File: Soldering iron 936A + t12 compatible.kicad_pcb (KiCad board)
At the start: 2 copper layers, 97 x 67 mm, 69 parts, among them J1 DC INPUT, J2 OLED, J3 AC input, J4 output_connector, J5 mosfet_driver_future_backup, J6 OLED, Q1 IRF9540N, Q2 BC547, SW1 RotaryEncoder_Switch, U1 LM2596S-ADJ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

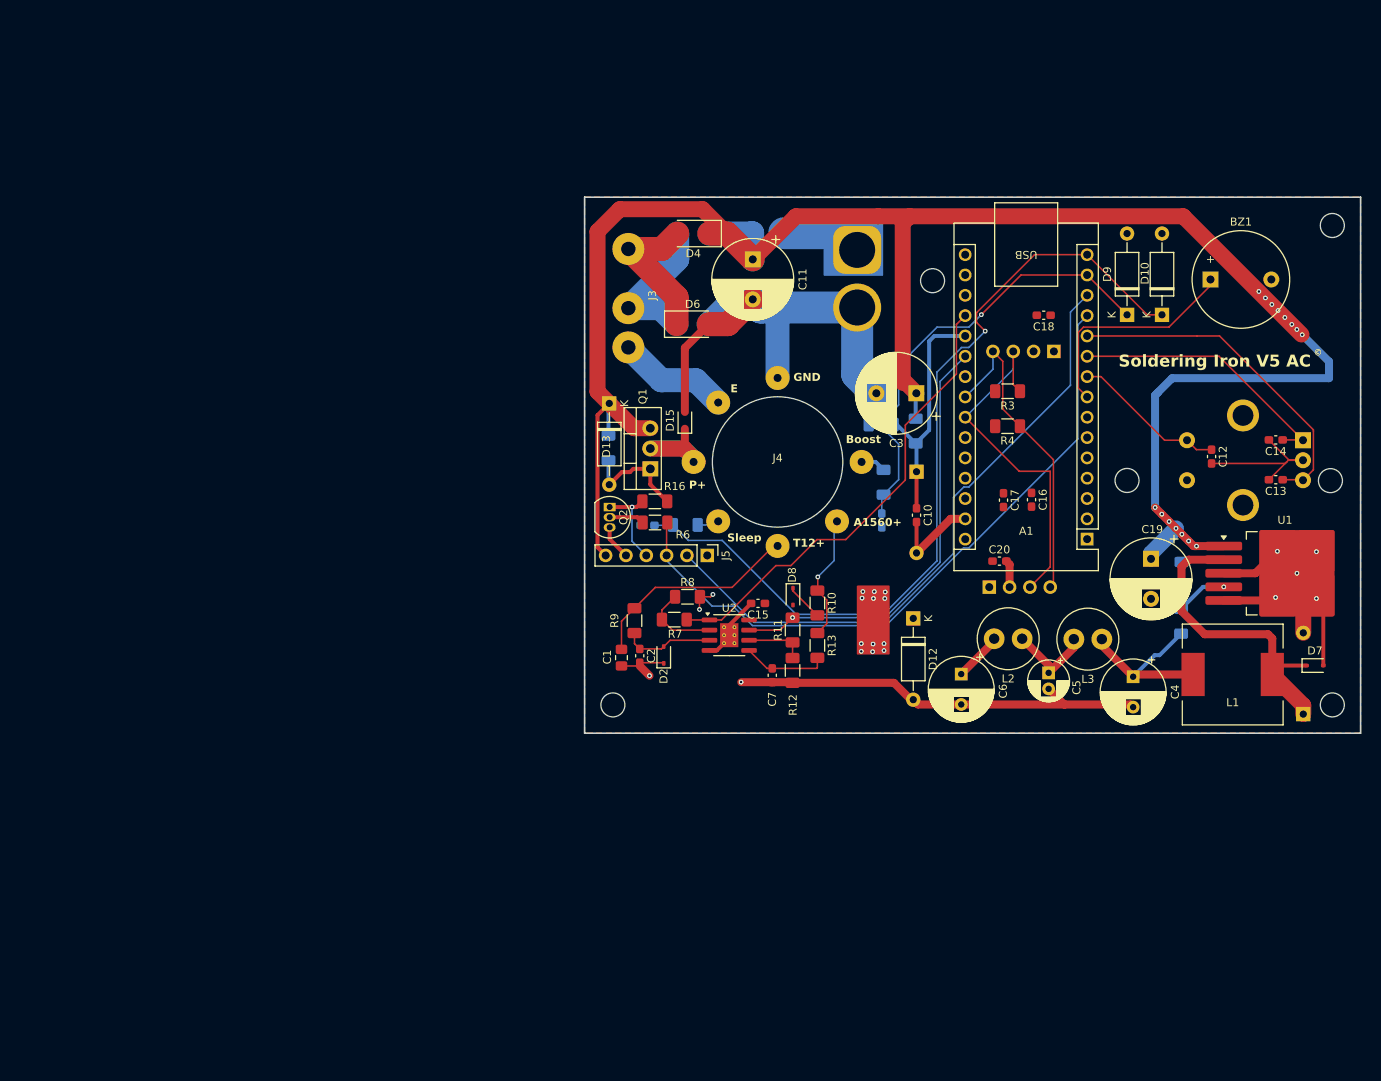
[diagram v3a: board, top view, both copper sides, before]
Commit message: added all 3d model files , almost finalised schematic , rough placment of big components
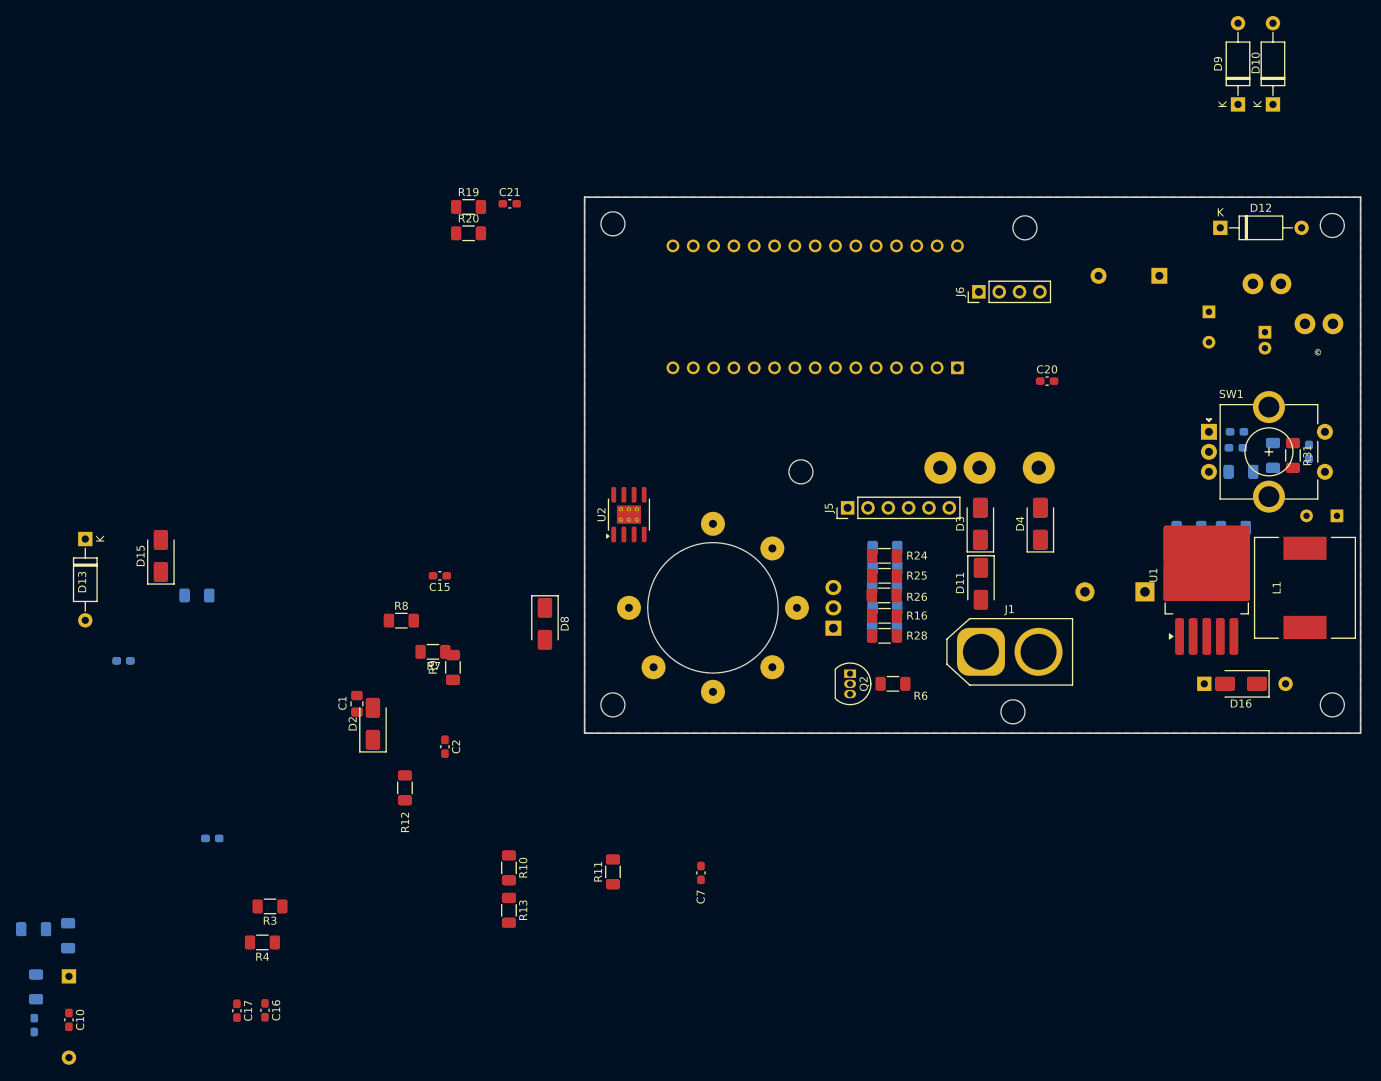
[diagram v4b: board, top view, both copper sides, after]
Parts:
- removed C11, C3: 1000uF, Capacitor_THT:CP_Radial_D10.0mm_P5.00mm
- removed D7: 1N5817WS, Diode_SMD:D_SOD-323
- removed J2: OLED, Connector_PinHeader_2.54mm:PinHeader_1x04_P2.54mm_Vertical
- added C21: 100nf, Capacitor_SMD:C_0603_1608Metric_Pad1.08x0.95mm_HandSolder, F.Cu at (161.6, 67.0)
- added D16: SS310, Diode_SMD:D_SMA, F.Cu at (253.0, 127.0)
- added R19: 5M, Resistor_SMD:R_1206_3216Metric_Pad1.30x1.75mm_HandSolder, F.Cu at (156.4, 67.4)
- added R20: 100, Resistor_SMD:R_1206_3216Metric_Pad1.30x1.75mm_HandSolder, F.Cu at (156.4, 70.7)
- added R21: 1.5k, Resistor_SMD:R_1206_3216Metric_Pad1.30x1.75mm_HandSolder, B.Cu at (208.5, 110.0)
- added R22: 1.5k, Resistor_SMD:R_1206_3216Metric_Pad1.30x1.75mm_HandSolder, B.Cu at (208.5, 112.5)
- added R23: 1.5k, Resistor_SMD:R_1206_3216Metric_Pad1.30x1.75mm_HandSolder, B.Cu at (208.4, 115.0)
- added R24: 3.3k, Resistor_SMD:R_1206_3216Metric_Pad1.30x1.75mm_HandSolder, F.Cu at (208.4, 111.0)
- added R25: 3.3k, Resistor_SMD:R_1206_3216Metric_Pad1.30x1.75mm_HandSolder, F.Cu at (208.4, 113.5)
- added R26: 3.3k, Resistor_SMD:R_1206_3216Metric_Pad1.30x1.75mm_HandSolder, F.Cu at (208.4, 116.0)
- added R27: 1.5k, Resistor_SMD:R_1206_3216Metric_Pad1.30x1.75mm_HandSolder, B.Cu at (208.5, 117.5)
- added R28: 3.3k, Resistor_SMD:R_1206_3216Metric_Pad1.30x1.75mm_HandSolder, F.Cu at (208.4, 121.0)
- added R29: 5k, Resistor_SMD:R_1206_3216Metric_Pad1.30x1.75mm_HandSolder, B.Cu at (257.0, 98.5)
- added R30: 5k, Resistor_SMD:R_1206_3216Metric_Pad1.30x1.75mm_HandSolder, B.Cu at (253.0, 100.5)
- added R31: 5k, Resistor_SMD:R_1206_3216Metric_Pad1.30x1.75mm_HandSolder, F.Cu at (259.5, 98.5)
- A1, BZ1, C12, C13, C14, C18, C4, C5, C6, D6, J3, J4, L2, L3, Q1: moved to B.Cu
- C19: footprint Capacitor_THT:CP_Radial_D10.0mm_P5.00mm -> Capacitor_THT:CP_Radial_D16.0mm_P7.50mm; moved to B.Cu
- D11, D3, J1, J6, SW1: moved to F.Cu
- D15, D2, D8: value 1N5817WS -> SS310; footprint Diode_SMD:D_SOD-323 -> Diode_SMD:D_SMA
- R16: value 10k -> 3.3k
- R5: value 10k -> 1.5k
- moved C8 123.3 mm to (102.2, 169.7)
- moved R2 123.3 mm to (106.4, 158.5)
- moved C10 123.3 mm to (106.5, 169.0)
- moved D1 123.3 mm to (106.5, 163.6)
- moved R1 123.3 mm to (102.1, 157.7)
- moved R14 123.3 mm to (102.4, 164.9)
- moved C18 122.8 mm to (124.4, 146.3), turned to 0 degrees
- moved C17 115.1 mm to (127.5, 167.9)
- moved C16 115.1 mm to (131.0, 167.8)
- moved R4 113.3 mm to (130.7, 159.3)
- moved R3 112.5 mm to (131.6, 154.8)
- moved C9 67.7 mm to (113.3, 124.1)
- moved D15 67.7 mm to (118.0, 111.0)
- moved D13 67.7 mm to (108.5, 108.9)
- moved D12 62.1 mm to (250.4, 70.0), turned to 0 degrees
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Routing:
- net /VIN: track 268.5 -> 0.00 mm, vias 15 -> 0
- net GND: track 200.1 -> 0.00 mm, vias 21 -> 0
- net Net-(A1-D12): track 106.5 -> 0.00 mm, vias 1 -> 0
- net /PWM: track 85.1 -> 0.00 mm
- net /PWM1: track 79.9 -> 0.00 mm
- net /temp_readback: track 58.2 -> 0.00 mm
- net Net-(A1-D11): track 56.0 -> 0.00 mm, vias 1 -> 0
- net /temp_readback_2: track 54.4 -> 0.00 mm, vias 1 -> 0
- net /SCL: track 45.0 -> 0.00 mm
- net /ENCODER B: track 42.6 -> 0.00 mm
- net /SDA: track 39.9 -> 0.00 mm
- net Net-(D14-K): track 39.8 -> 0.00 mm
- net /ENCODER A: track 33.9 -> 0.00 mm
- net /VIN_ADC: track 30.1 -> 0.00 mm
- net /BUZZER: track 28.2 -> 0.00 mm
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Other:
- outline, holes or cut-outs redrawn
- board text removed: "A1560+"
- board text removed: "Boost"
- board text removed: "E"
- board text removed: "GND"
- board text removed: "P+"
- board text removed: "Sleep"
- board text removed: "T12+"

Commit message: Finalised schematic , placement
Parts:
- added 5V1: TestPoint, TestPoint:TestPoint_Pad_D1.0mm, B.Cu at (229.5, 69.0)
- added C11: 100nf, Capacitor_SMD:C_0603_1608Metric_Pad1.08x0.95mm_HandSolder, F.Cu at (202.4, 128.5)
- added C22: 1nf, Capacitor_SMD:C_0603_1608Metric_Pad1.08x0.95mm_HandSolder, F.Cu at (204.1, 131.0)
- added C23: 100nf, Capacitor_SMD:C_0603_1608Metric_Pad1.08x0.95mm_HandSolder, B.Cu at (197.6, 132.0)
- added C24: 1000uF, Capacitor_THT:CP_Radial_D16.0mm_P7.50mm, B.Cu at (243.0, 97.5)
- added C25: 100nf, Capacitor_SMD:C_0603_1608Metric_Pad1.08x0.95mm_HandSolder, F.Cu at (174.0, 96.5)
- added C26: 1uF, Capacitor_SMD:C_0603_1608Metric_Pad1.08x0.95mm_HandSolder, F.Cu at (191.4, 100.0)
- added D17: SS310, Diode_SMD:D_SMA, B.Cu at (192.5, 100.0)
- added D18: SS310, Diode_SMD:D_SMA, B.Cu at (203.5, 98.0)
- added D19: SS310, Diode_SMD:D_SMA, F.Cu at (196.0, 105.0)
- added D7: SS310, Diode_SMD:D_SMA, B.Cu at (177.0, 100.0)
- added F1: Fuse, Fuse:Fuse_1206_3216Metric_Pad1.42x1.75mm_HandSolder, F.Cu at (209.6, 101.5)
- added GND1: TestPoint, TestPoint:TestPoint_Pad_D1.0mm, B.Cu at (233.5, 69.0)
- added J2: USB TO SERIAL, Connector_PinHeader_2.54mm:PinHeader_1x04_P2.54mm_Vertical, B.Cu at (173.5, 76.0)
- added J7: USB C BREAKOUT BOARD, Connector_PinHeader_2.54mm:PinHeader_1x08_P2.54mm_Vertical, F.Cu at (194.6, 96.0)
- added PWM1: TestPoint, TestPoint:TestPoint_Pad_D1.0mm, B.Cu at (190.5, 92.0)
- added R32: 22.6K, Resistor_SMD:R_1206_3216Metric_Pad1.30x1.75mm_HandSolder, F.Cu at (183.0, 100.5)
- added R33: 10k, Resistor_SMD:R_1206_3216Metric_Pad1.30x1.75mm_HandSolder, F.Cu at (186.3, 100.5)
- added R34: 5.1K, Resistor_SMD:R_1206_3216Metric_Pad1.30x1.75mm_HandSolder, B.Cu at (175.4, 92.5)
- added R35: 1M, Resistor_SMD:R_1206_3216Metric_Pad1.30x1.75mm_HandSolder, F.Cu at (209.6, 98.5)
- added R36: 220k, Resistor_SMD:R_1206_3216Metric_Pad1.30x1.75mm_HandSolder, B.Cu at (209.4, 101.5)
- added R37: 10K, Resistor_SMD:R_1206_3216Metric_Pad1.30x1.75mm_HandSolder, F.Cu at (200.5, 91.5)
- added R38: 5.1K, Resistor_SMD:R_1206_3216Metric_Pad1.30x1.75mm_HandSolder, B.Cu at (185.4, 92.5)
- added SCL1: TestPoint, TestPoint:TestPoint_Pad_D1.0mm, B.Cu at (224.5, 74.5)
- added SDA1: TestPoint, TestPoint:TestPoint_Pad_D1.0mm, B.Cu at (228.0, 74.5)
- added U3: ACS712xLCTR-05B, Package_SO:SOIC-8_3.9x4.9mm_P1.27mm, B.Cu at (202.4, 128.0)
- added U4: HUSB238, Package_DFN_QFN:DFN-10-1EP_3x3mm_P0.5mm_EP1.58x2.35mm, B.Cu at (184.9, 101.1)
- added U5: PC817, Package_DIP:DIP-4_W7.62mm, F.Cu at (202.0, 101.5)
- added VBUS1: TestPoint, TestPoint:TestPoint_Pad_D1.0mm, B.Cu at (189.5, 105.5)
- C1, C15, C2, C21, D15, D2, J5, Q2, R20, R6: moved to B.Cu
- D1, R1, R14, R15, R2: moved to F.Cu
- D13: footprint Diode_THT:D_A-405_P10.16mm_Horizontal -> Diode_THT:D_A-405_P2.54mm_Vertical_KathodeUp; moved to B.Cu
- moved C10 143.2 mm to (235.6, 107.0), turned to 180 degrees
- moved R1 141.8 mm to (235.4, 109.5)
- moved R2 141.3 mm to (239.5, 111.1), turned to 90 degrees
- moved R4 123.6 mm to (228.0, 83.0), turned to -90 degrees
- moved C17 123.0 mm to (208.5, 75.4)
- moved D1 122.0 mm to (192.4, 77.0), turned to 0 degrees
- moved C16 121.9 mm to (210.5, 75.4)
- moved R3 118.2 mm to (225.5, 83.0), turned to -90 degrees
- moved C18 117.1 mm to (221.6, 81.0)
- moved D13 91.0 mm to (199.5, 110.5)
- moved D15 90.6 mm to (207.0, 128.0), turned to -90 degrees
- moved C8 87.9 mm to (176.0, 122.0), turned to 90 degrees
- moved R14 85.2 mm to (176.0, 122.1)
- moved C9 82.6 mm to (195.9, 128.0)
- moved D10 81.9 mm to (181.0, 85.1)
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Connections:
- A1 pad 22: unconnected-(A1-A3-Pad22) -> /current_sense
- A1 pad 7: unconnected-(A1-D4-Pad7) -> /LEAK_ERR
- D15 pad 1: /P+ -> /MOS_OUT
- J4 pad 6: Earth -> Net-(D18-A)
- Q1 pad 2: /P+ -> /MOS_OUT
- R20 pad 1: /P+ -> /MOS_OUT
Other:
- outline, holes or cut-outs redrawn

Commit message: Almost completed layout , checks pending
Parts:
- C10, F1, R1, R2, R37: moved to B.Cu
- R36: value 220k -> 50K; moved to F.Cu
- moved R2 25.2 mm to (242.2, 86.0)
- moved R1 23.8 mm to (239.5, 86.0), turned to -90 degrees
- moved C10 20.4 mm to (237.0, 86.7), turned to 90 degrees
- moved D2 13.1 mm to (181.5, 131.0), turned to 180 degrees
- moved D14 9.83 mm to (258.2, 127.0), turned to 180 degrees
- moved C19 5.67 mm to (237.0, 111.5), turned to -90 degrees
- moved C1 5.00 mm to (188.0, 131.0), turned to 0 degrees
- moved C26 2.41 mm to (189.0, 99.5), turned to 90 degrees
- moved VBUS1 1.58 mm to (191.0, 105.0)
- moved R37 0.75 mm to (200.5, 90.8)
- moved R36 0.05 mm to (209.5, 101.5)
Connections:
- U4 pad 2: Net-(D17-K) -> unconnected-(U4-D+-Pad2)
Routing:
- net /current_sense: track 0.00 -> 116.4 mm
- net /VIN: track 0.00 -> 115.7 mm, vias 0 -> 3
- net /SDA: track 0.00 -> 107.8 mm, vias 0 -> 2
- net /SCL: track 0.00 -> 101.4 mm, vias 0 -> 2
- net /PWM: track 0.00 -> 85.9 mm
- net Net-(A1-D12): track 0.00 -> 83.6 mm, vias 0 -> 3
- net /ENCODER S: track 0.00 -> 76.8 mm
- net /ENCODER B: track 0.00 -> 68.2 mm
- net /ENCODER A: track 0.00 -> 66.8 mm
- net GND: track 0.00 -> 62.0 mm, vias 0 -> 64
- net /VIN_ADC: track 0.00 -> 60.4 mm
- net Net-(A1-D11): track 0.00 -> 56.3 mm
- net /BUZZER: track 0.00 -> 51.3 mm
- net /temp_readback: track 0.00 -> 47.7 mm
- net /temp_readback_2: track 0.00 -> 44.3 mm
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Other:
- outline, holes or cut-outs redrawn

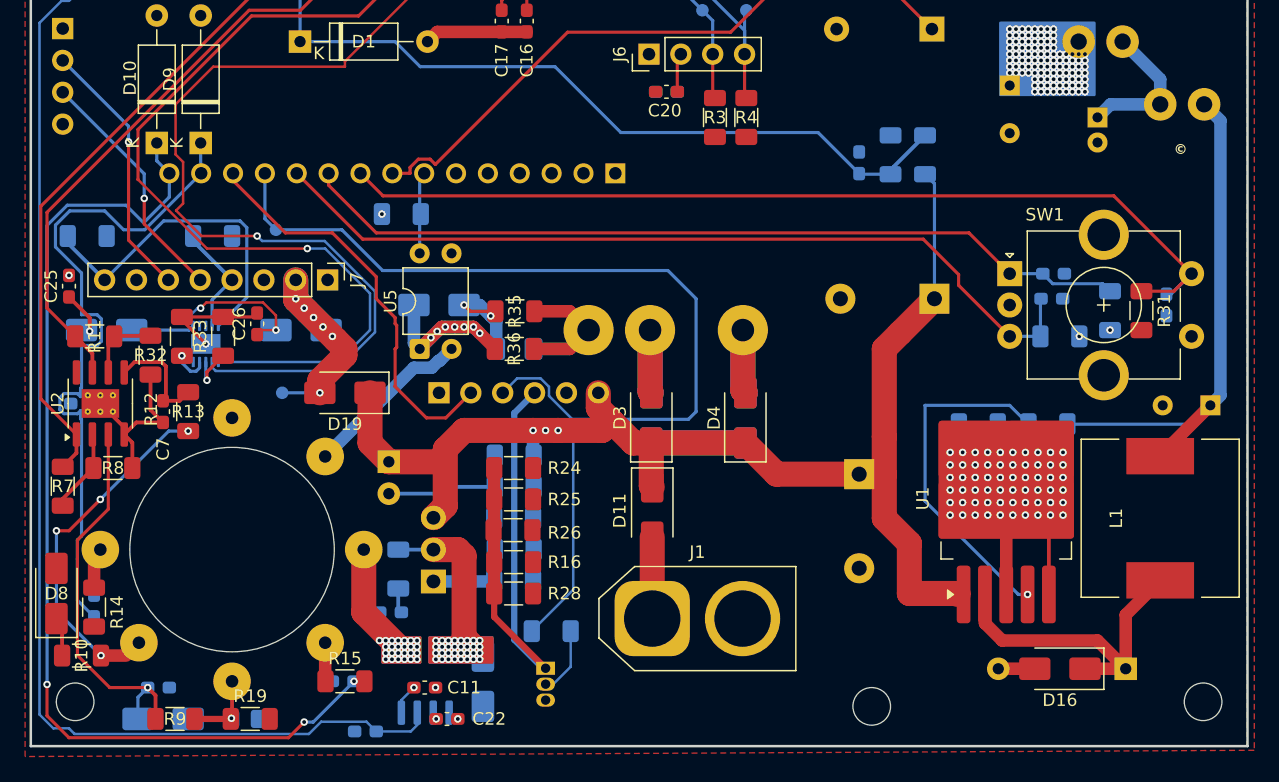
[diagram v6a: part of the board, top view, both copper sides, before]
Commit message: Layout fully complete yet to be reviewed
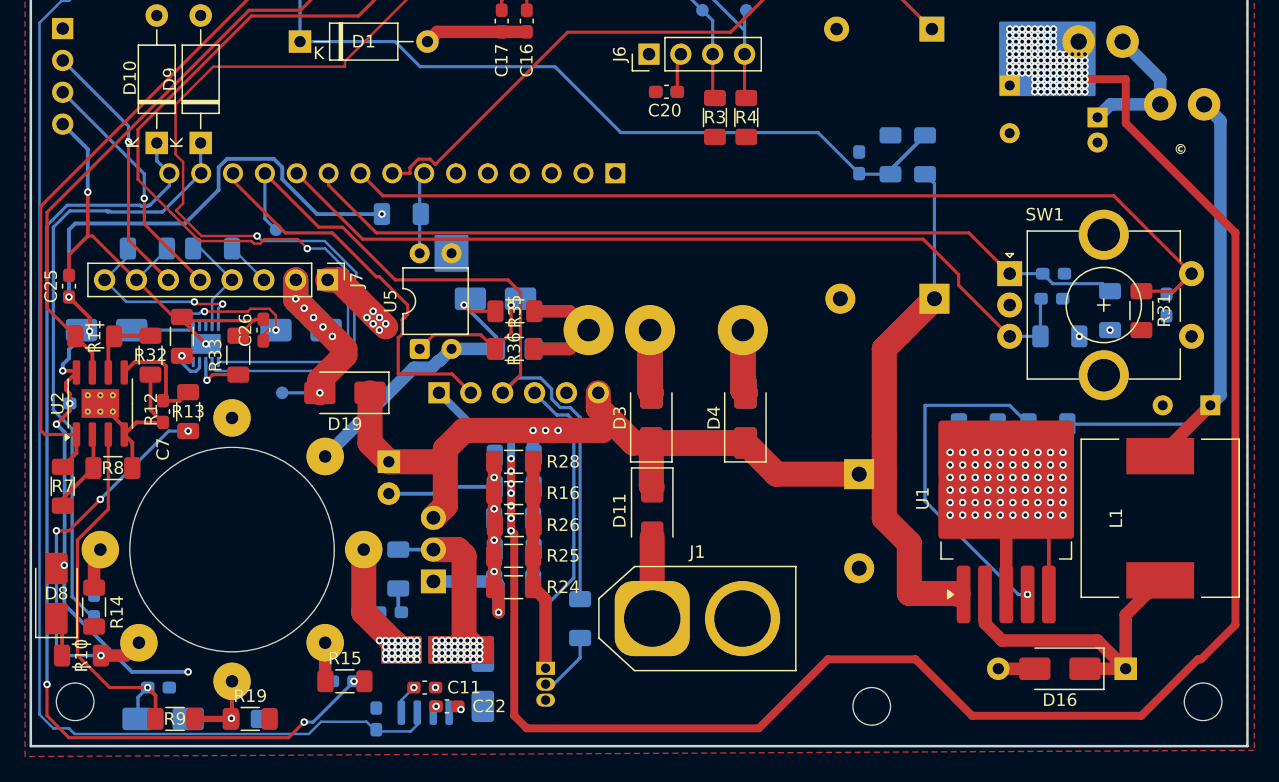
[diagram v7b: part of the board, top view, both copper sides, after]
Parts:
- moved R28 10.5 mm to (209.4, 110.5), turned to 180 degrees
- moved R24 9.50 mm to (209.4, 120.5), turned to 180 degrees
- moved R16 5.50 mm to (209.4, 113.0), turned to 180 degrees
- moved R34 4.90 mm to (180.2, 93.5)
- moved D18 4.53 mm to (208.0, 97.5), turned to 180 degrees
- moved R25 4.50 mm to (209.4, 118.0), turned to 180 degrees
- moved R6 2.51 mm to (214.8, 123.0), turned to -90 degrees
- moved R33 1.93 mm to (187.5, 102.0)
- moved C23 1.32 mm to (198.5, 131.0), turned to -90 degrees
- moved C22 1.00 mm to (204.1, 130.0)
- moved R38 1.00 mm to (185.4, 93.5)
- moved C26 0.71 mm to (189.5, 100.0)
- moved R26 0.41 mm to (209.5, 115.5), turned to 180 degrees
- moved C15 0.08 mm to (174.9, 105.8)
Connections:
- J7 pad 3: unconnected-(J7-SUB2-Pad3) -> GND
- J7 pad 7: unconnected-(J7-SUB1-Pad7) -> GND
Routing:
- net +5V: track 14.0 -> 238.7 mm, vias 117 -> 130
- net GND: track 62.0 -> 102.5 mm, vias 64 -> 70
- net /PWM: track 85.9 -> 60.7 mm
- net Net-(D13-A): track 23.6 -> 38.2 mm, vias 0 -> 5
- net /CC2: track 27.0 -> 15.4 mm, vias 0 -> 2
- net Net-(A1-D11): track 56.3 -> 48.8 mm
- net Net-(D18-K): track 17.2 -> 12.8 mm, vias 7 -> 1
- net Net-(D18-A): track 21.6 -> 24.5 mm, vias 2 -> 1
- net /thermocouple_a1560 +: track 28.7 -> 30.5 mm
- net /PWM1: track 32.6 -> 30.8 mm
- net Net-(A1-D12): track 83.6 -> 81.9 mm
- net /temp_readback: track 47.7 -> 49.2 mm
- net /SCL: track 101.4 -> 100.2 mm
- net /SDA: track 107.8 -> 106.6 mm
- net Net-(D17-K): track 16.3 -> 15.5 mm
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
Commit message: Review 5V and GND planes
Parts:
- C18: moved to F.Cu
- moved C8 13.3 mm to (176.5, 108.8), turned to 0 degrees
- moved C18 1.75 mm to (221.6, 82.8)
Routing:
- net GND: track 102.5 -> 107.1 mm
- net Net-(A1-D11): track 48.8 -> 52.0 mm, vias 0 -> 1
- net /VIN_USBC: track 19.5 -> 20.1 mm
- net +5V: vias 130 -> 19
